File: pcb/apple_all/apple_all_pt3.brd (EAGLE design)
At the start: 56 x 65 mm, 50 parts, among them IC1 STM32F072C8T6, SW1 324_SW, SW2 324_SW, SW3 324_SW

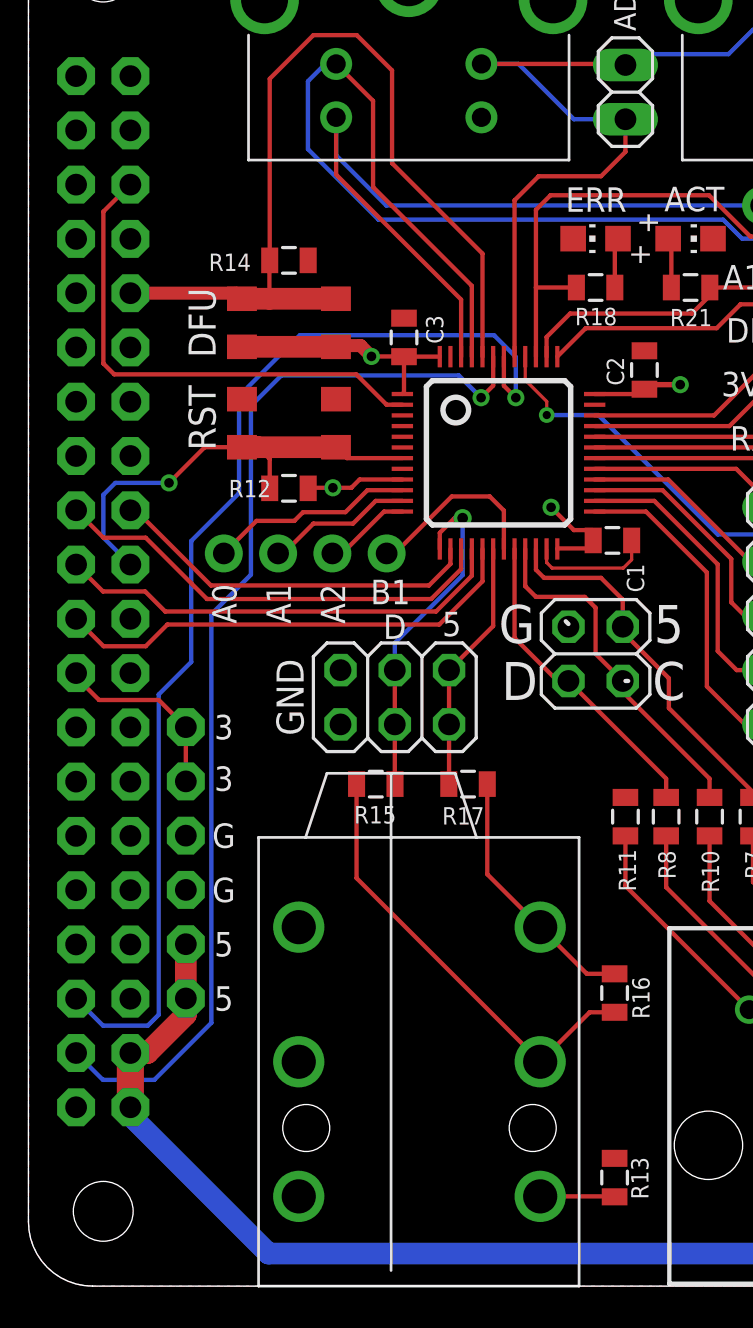
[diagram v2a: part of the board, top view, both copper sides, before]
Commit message: added busy pin and adjusted resistors
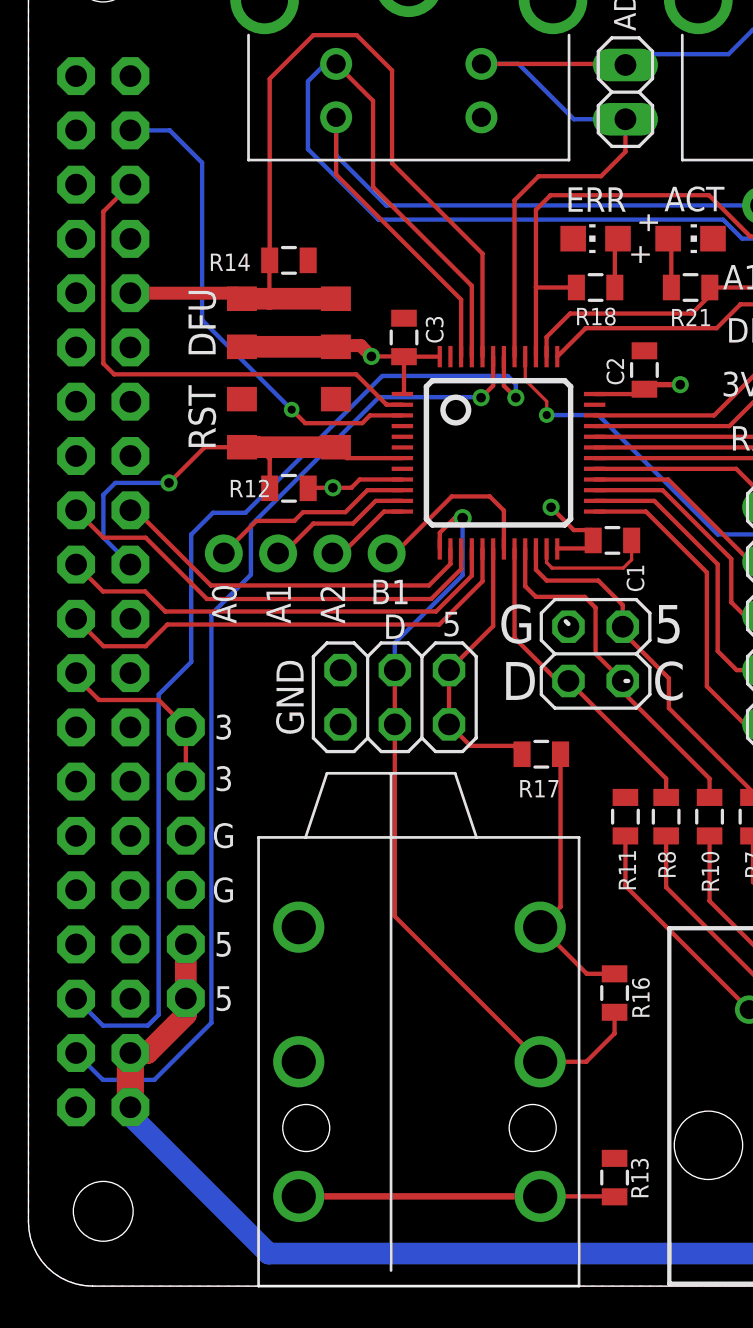
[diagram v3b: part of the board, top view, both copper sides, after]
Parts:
- removed R15: 100, SparkFun-Passives:0805
- moved R17 3.70 mm to (24.0, 24.9)
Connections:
- removed net N$41: IC1.13, JP5.3, JP5.4, R15.2
- new net N$33: IC1.3, JP4.38
- net N$24: now also JP6.SLEEVE-NORM
- net N$30: now also IC1.13, JP5.3, JP5.4; no longer R15.1
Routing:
- net N$33: track 0.00 -> 22.9 mm, vias 0 -> 1
- net N$41: track 15.9 -> 0.00 mm, vias 1 -> 0
- net N$30: track 21.0 -> 36.7 mm, vias 0 -> 1
- net N$24: track 3.49 -> 14.8 mm
- net N$22: track 53.7 -> 48.9 mm
- net N$23: track 51.5 -> 47.4 mm
- net N$31: track 11.9 -> 13.1 mm
- net N$32: track 12.1 -> 12.9 mm
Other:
- board text added: "PT5 dekuNukem MAR2023"
- board text removed: "PT4 dekuNukem DEC2022"
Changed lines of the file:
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@@
 Apple Lisa, Early Macintosh
 &amp; Apple Desktop Bus</text>
-<text x="40.8178" y="10.6426" size="1.6764" layer="26" rot="MR180" align="center">PT4 dekuNukem DEC2022</text>
+<text x="40.8178" y="10.6426" size="1.6764" layer="26" rot="MR180" align="center">PT5 dekuNukem MAR2023</text>
 <text x="37.3888" y="3.1496" size="1.9304" layer="26" rot="MR180" align="center">usb4vc.com</text>
 <wire x1="27.94" y1="28.321" x2="28.067" y2="28.321" width="0.2032" layer="21"/>
@@
 <attribute name="NAME" x="48.895" y="64.8335" size="0.8128" layer="25" rot="R180"/>
 </element>
-<element name="R15" library="SparkFun-Passives" package="0805" value="100" x="16.256" y="23.495" smashed="yes">
-<attribute name="NAME" x="15.24" y="21.6535" size="0.8128" layer="25"/>
-</element>
-<element name="R17" library="SparkFun-Passives" package="0805" value="100" x="20.574" y="23.495" smashed="yes" rot="R180">
-<attribute name="NAME" x="21.336" y="22.4155" size="0.8128" layer="25" rot="R180"/>
+<element name="R17" library="SparkFun-Passives" package="0805" value="100" x="24.003" y="24.892" smashed="yes" rot="R180">
+<attribute name="NAME" x="24.892" y="23.6855" size="0.8128" layer="25" rot="R180"/>
 </element>
 </elements>
@@
 <wire x1="22.25" y1="42.139" x2="22.8092" y2="41.5798" width="0.2032" layer="1"/>
 <via x="22.8092" y="41.5798" extent="1-16" drill="0.45"/>
-<wire x1="22.8092" y1="41.5798" x2="22.8092" y2="43.4848" width="0.2032" layer="16"/>
-<wire x1="22.8092" y1="43.4848" x2="21.7932" y2="44.5008" width="0.2032" layer="16"/>
+<wire x1="22.8092" y1="41.5798" x2="22.8092" y2="42.2148" width="0.2032" layer="16"/>
+<wire x1="22.8092" y1="42.2148" x2="22.4282" y2="42.5958" width="0.2032" layer="16"/>
 <wire x1="3.488" y1="12.192" x2="2.23" y2="13.45" width="0.2032" layer="16"/>
-<wire x1="21.7932" y1="44.5008" x2="12.7" y2="44.5008" width="0.2032" layer="16"/>
-<wire x1="12.7" y1="44.5008" x2="9.8552" y2="41.656" width="0.2032" layer="16"/>
-<wire x1="9.8552" y1="37.1094" x2="7.62" y2="34.8742" width="0.2032" layer="16"/>
-<wire x1="9.8552" y1="41.656" x2="9.8552" y2="37.1094" width="0.2032" layer="16"/>
-<wire x1="7.62" y1="34.8742" x2="7.62" y2="29.21" width="0.2032" layer="16"/>
 <wire x1="6.096" y1="27.686" x2="6.096" y2="12.7" width="0.2032" layer="16"/>
 <wire x1="6.096" y1="12.7" x2="5.588" y2="12.192" width="0.2032" layer="16"/>
 <wire x1="5.588" y1="12.192" x2="3.488" y2="12.192" width="0.2032" layer="16"/>
 <wire x1="7.62" y1="29.21" x2="6.096" y2="27.686" width="0.2032" layer="16"/>
+<wire x1="22.4282" y1="42.5958" x2="16.5608" y2="42.5958" width="0.2032" layer="16"/>
+<wire x1="10.16" y1="36.195" x2="8.636" y2="36.195" width="0.2032" layer="16"/>
+<wire x1="8.636" y1="36.195" x2="7.62" y2="35.179" width="0.2032" layer="16"/>
+<wire x1="16.5608" y1="42.5958" x2="10.16" y2="36.195" width="0.2032" layer="16"/>
+<wire x1="7.62" y1="35.179" x2="7.62" y2="29.21" width="0.2032" layer="16"/>
 </signal>
 <signal name="N$23">
@@
 <wire x1="21.75" y1="42.1462" x2="21.1836" y2="41.5798" width="0.2032" layer="1"/>
 <via x="21.1836" y="41.5798" extent="1-16" drill="0.45"/>
-<wire x1="21.1836" y1="41.5798" x2="20.1422" y2="42.6212" width="0.2032" layer="16"/>
-<wire x1="20.1422" y1="42.6212" x2="11.8364" y2="42.6212" width="0.2032" layer="16"/>
-<wire x1="11.8364" y1="42.6212" x2="10.414" y2="41.1988" width="0.2032" layer="16"/>
+<wire x1="21.1836" y1="41.5798" x2="21.1582" y2="41.6052" width="0.2032" layer="16"/>
+<wire x1="21.1582" y1="41.6052" x2="16.4084" y2="41.6052" width="0.2032" layer="16"/>
+<wire x1="16.4084" y1="41.6052" x2="10.414" y2="35.6108" width="0.2032" layer="16"/>
 <wire x1="3.488" y1="9.652" x2="2.23" y2="10.91" width="0.2032" layer="16"/>
 <wire x1="5.8928" y1="9.652" x2="3.488" y2="9.652" width="0.2032" layer="16"/>
-<wire x1="10.414" y1="41.1988" x2="10.414" y2="33.2994" width="0.2032" layer="16"/>
+<wire x1="10.414" y1="35.6108" x2="10.414" y2="33.2994" width="0.2032" layer="16"/>
 <wire x1="10.414" y1="33.2994" x2="8.5598" y2="31.4452" width="0.2032" layer="16"/>
 <wire x1="8.5598" y1="31.4452" x2="8.5598" y2="12.319" width="0.2032" layer="16"/>
@@
 <wire x1="14.6812" y1="34.29" x2="14.224" y2="34.29" width="0.2032" layer="1"/>
 <wire x1="14.6812" y1="34.29" x2="16.6412" y2="36.25" width="0.2032" layer="1"/>
-</signal>
-<signal name="N$41">
-<contactref element="IC1" pad="13"/>
-<contactref element="JP5" pad="3"/>
-<contactref element="JP5" pad="4"/>
-<wire x1="17.145" y1="26.289" x2="17.145" y2="28.829" width="0.2032" layer="1"/>
-<wire x1="19.25" y1="34.5" x2="19.25" y2="35.252" width="0.2032" layer="1"/>
-<wire x1="19.939" y1="35.941" x2="20.32" y2="35.941" width="0.2032" layer="1"/>
-<wire x1="19.939" y1="35.941" x2="19.25" y2="35.252" width="0.2032" layer="1"/>
-<via x="20.32" y="35.941" extent="1-16" drill="0.5"/>
-<wire x1="20.32" y1="35.941" x2="20.32" y2="33.274" width="0.2032" layer="16"/>
-<wire x1="17.145" y1="30.099" x2="17.145" y2="28.829" width="0.2032" layer="16"/>
-<wire x1="20.32" y1="33.274" x2="17.145" y2="30.099" width="0.2032" layer="16"/>
-<contactref element="R15" pad="2"/>
-<wire x1="17.145" y1="26.289" x2="17.145" y2="23.506" width="0.2032" layer="1"/>
-<wire x1="17.145" y1="23.506" x2="17.156" y2="23.495" width="0.2032" layer="1"/>
 </signal>
 <signal name="N$3">
@@
 <contactref element="IC1" pad="22"/>
 <wire x1="23.75" y1="34.5" x2="23.75" y2="33.527" width="0.2032" layer="1"/>
-<wire x1="23.75" y1="33.527" x2="24.13" y2="33.147" width="0.2032" layer="1"/>
-<wire x1="24.13" y1="33.147" x2="26.797" y2="33.147" width="0.2032" layer="1"/>
-<wire x1="26.797" y1="33.147" x2="27.813" y2="32.131" width="0.2032" layer="1"/>
-<wire x1="27.813" y1="32.131" x2="27.813" y2="30.861" width="0.2032" layer="1"/>
+<wire x1="23.75" y1="33.527" x2="24.257" y2="33.02" width="0.2032" layer="1"/>
+<wire x1="24.257" y1="33.02" x2="26.67" y2="33.02" width="0.2032" layer="1"/>
+<wire x1="26.67" y1="33.02" x2="27.813" y2="31.877" width="0.2032" layer="1"/>
+<wire x1="27.813" y1="31.877" x2="27.813" y2="30.861" width="0.2032" layer="1"/>
 <wire x1="27.813" y1="30.861" x2="27.813" y2="30.607" width="0.2032" layer="1"/>
 <wire x1="27.813" y1="30.607" x2="29.972" y2="28.448" width="0.2032" layer="1"/>
@@
 <wire x1="21.75" y1="30.894" x2="21.75" y2="34.5" width="0.2032" layer="1"/>
 <contactref element="R17" pad="2"/>
-<wire x1="19.685" y1="26.289" x2="19.685" y2="23.506" width="0.2032" layer="1"/>
-<wire x1="19.685" y1="23.506" x2="19.674" y2="23.495" width="0.2032" layer="1"/>
+<wire x1="19.685" y1="26.289" x2="20.69" y2="25.284" width="0.2032" layer="1"/>
+<wire x1="23.103" y1="24.892" x2="22.711" y2="25.284" width="0.2032" layer="1"/>
+<wire x1="22.711" y1="25.284" x2="20.69" y2="25.284" width="0.2032" layer="1"/>
 </signal>
 <signal name="N$24">
@@
 <wire x1="23.95" y1="4.2" x2="27.412" y2="4.2" width="0.2032" layer="1"/>
 <wire x1="27.412" y1="4.2" x2="27.432" y2="4.18" width="0.2032" layer="1"/>
+<contactref element="JP6" pad="SLEEVE-NORM"/>
+<wire x1="12.65" y1="4.2" x2="23.95" y2="4.2" width="0.3048" layer="1"/>
 </signal>
 <signal name="N$11">
@@
 <contactref element="JP6" pad="RING"/>
 <contactref element="R16" pad="2"/>
-<wire x1="27.432" y1="12.816" x2="26.266" y2="12.816" width="0.2032" layer="1"/>
-<wire x1="26.266" y1="12.816" x2="23.95" y2="10.5" width="0.2032" layer="1"/>
-<contactref element="R15" pad="1"/>
-<wire x1="15.356" y1="23.495" x2="15.356" y2="19.094" width="0.2032" layer="1"/>
-<wire x1="15.356" y1="19.094" x2="23.95" y2="10.5" width="0.2032" layer="1"/>
+<wire x1="27.432" y1="12.816" x2="27.432" y2="11.823" width="0.2032" layer="1"/>
+<wire x1="27.432" y1="11.823" x2="26.109" y2="10.5" width="0.2032" layer="1"/>
+<wire x1="26.109" y1="10.5" x2="23.95" y2="10.5" width="0.2032" layer="1"/>
+<contactref element="IC1" pad="13"/>
+<contactref element="JP5" pad="3"/>
+<contactref element="JP5" pad="4"/>
+<wire x1="17.145" y1="26.289" x2="17.145" y2="28.829" width="0.2032" layer="1"/>
+<wire x1="19.25" y1="34.5" x2="19.25" y2="35.252" width="0.2032" layer="1"/>
+<wire x1="19.939" y1="35.941" x2="20.32" y2="35.941" width="0.2032" layer="1"/>
+<wire x1="19.939" y1="35.941" x2="19.25" y2="35.252" width="0.2032" layer="1"/>
+<via x="20.32" y="35.941" extent="1-16" drill="0.5"/>
+<wire x1="20.32" y1="35.941" x2="20.32" y2="33.274" width="0.2032" layer="16"/>
+<wire x1="17.145" y1="30.099" x2="17.145" y2="28.829" width="0.2032" layer="16"/>
+<wire x1="20.32" y1="33.274" x2="17.145" y2="30.099" width="0.2032" layer="16"/>
+<wire x1="17.145" y1="17.305" x2="23.95" y2="10.5" width="0.2032" layer="1"/>
+<wire x1="17.145" y1="26.289" x2="17.145" y2="17.305" width="0.2032" layer="1"/>
 </signal>
 <signal name="N$32">
@@
 <wire x1="26.134" y1="14.616" x2="27.432" y2="14.616" width="0.2032" layer="1"/>
 <contactref element="R17" pad="1"/>
-<wire x1="21.474" y1="23.495" x2="21.474" y2="19.276" width="0.2032" layer="1"/>
-<wire x1="21.474" y1="19.276" x2="23.95" y2="16.8" width="0.2032" layer="1"/>
+<wire x1="24.903" y1="24.892" x2="24.903" y2="17.753" width="0.2032" layer="1"/>
+<wire x1="24.903" y1="17.753" x2="23.95" y2="16.8" width="0.2032" layer="1"/>
+</signal>
+<signal name="N$33">
+<contactref element="IC1" pad="3"/>
+<contactref element="JP4" pad="38"/>
+<wire x1="17.5" y1="40.75" x2="15.985" y2="40.75" width="0.2032" layer="1"/>
+<wire x1="15.985" y1="40.75" x2="15.621" y2="40.386" width="0.2032" layer="1"/>
+<wire x1="15.621" y1="40.386" x2="12.954" y2="40.386" width="0.2032" layer="1"/>
+<wire x1="12.954" y1="40.386" x2="12.319" y2="41.021" width="0.2032" layer="1"/>
+<via x="12.319" y="41.021" extent="1-16" drill="0.381"/>
+<wire x1="12.319" y1="41.021" x2="8.128" y2="45.212" width="0.2032" layer="16"/>
+<wire x1="8.128" y1="45.212" x2="8.128" y2="52.578" width="0.2032" layer="16"/>
+<wire x1="8.128" y1="52.578" x2="6.616" y2="54.09" width="0.2032" layer="16"/>
+<wire x1="6.616" y1="54.09" x2="4.77" y2="54.09" width="0.2032" layer="16"/>
 </signal>
 </signals>
